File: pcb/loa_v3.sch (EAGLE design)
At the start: 111 parts, among them IC1 STM32F10XVXT6, IC2 M25P80MW, IC3 NAND_FLASH, IC4 MCP1825S-1202E/DB, IC5 NCP3170, IC6 AD7266SU, Q2 50.000, Q3 25.000, U1 6SLX9TQG144, X3 MINI-USB

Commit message: Cleanup
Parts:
- JP8: value (none) -> GND
- SJ2: value (none) -> WP
- SJ3: value (none) -> AGND-GND
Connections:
- net N$37 renamed VDDA
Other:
- moved on the sheet: R12, R13

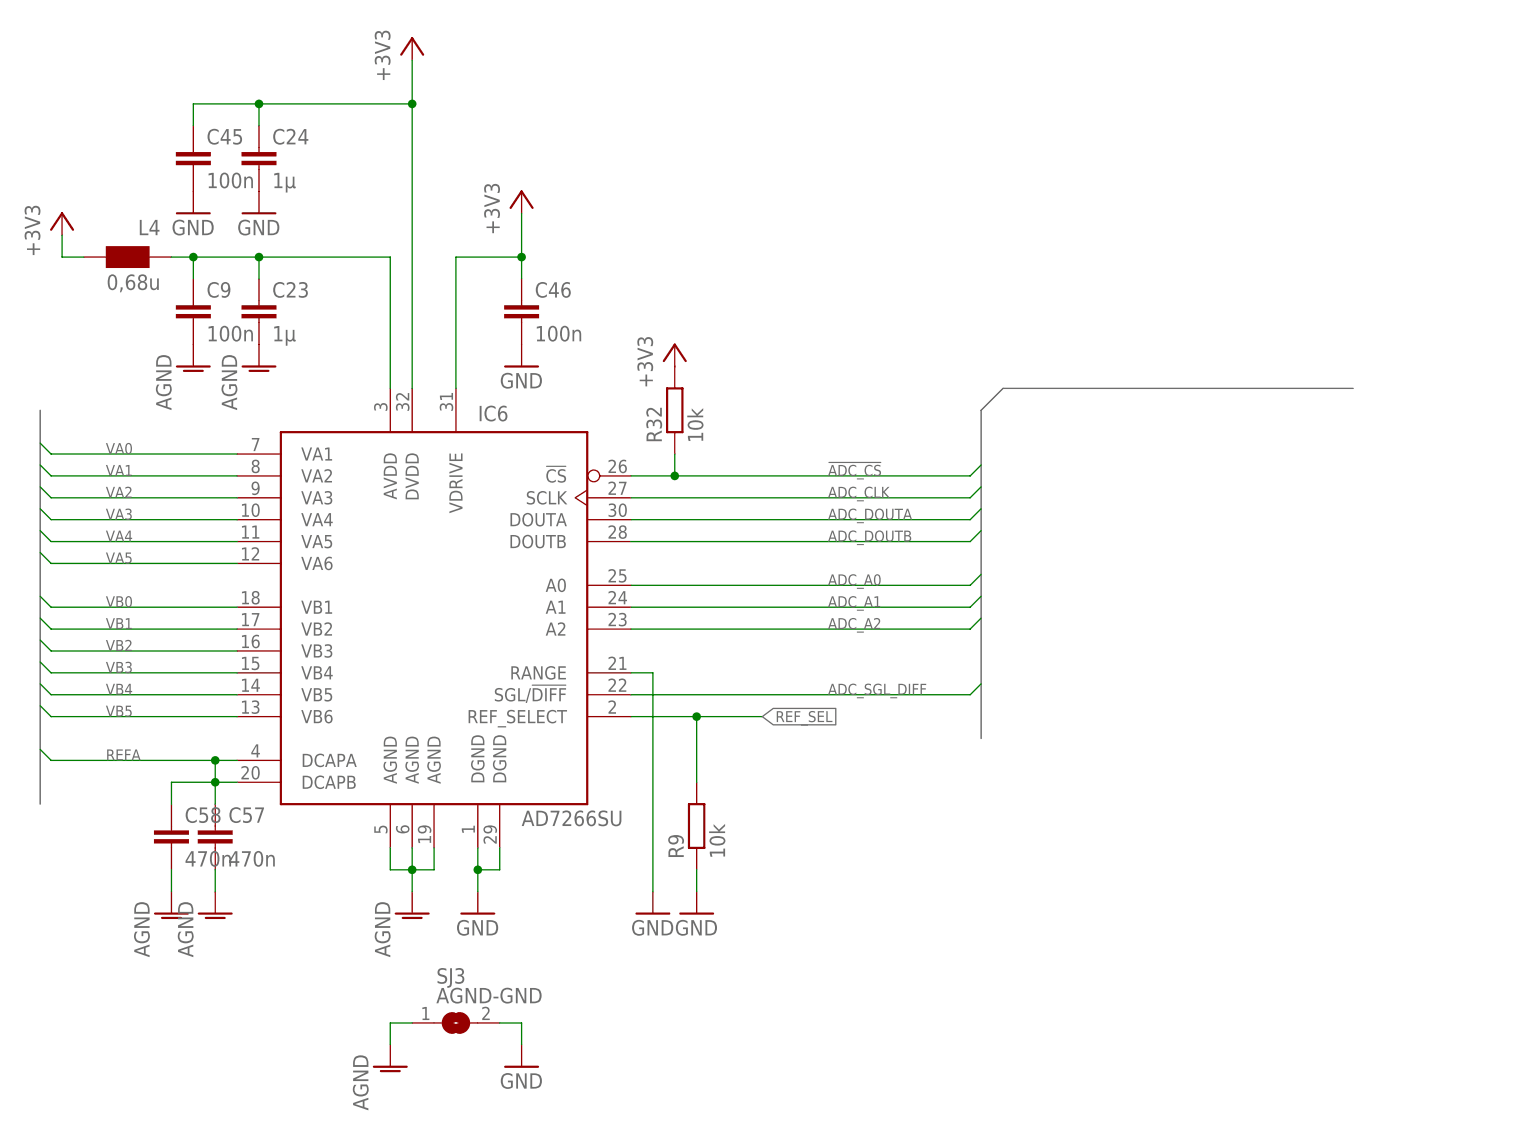
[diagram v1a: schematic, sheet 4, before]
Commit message: Added BOM attributes
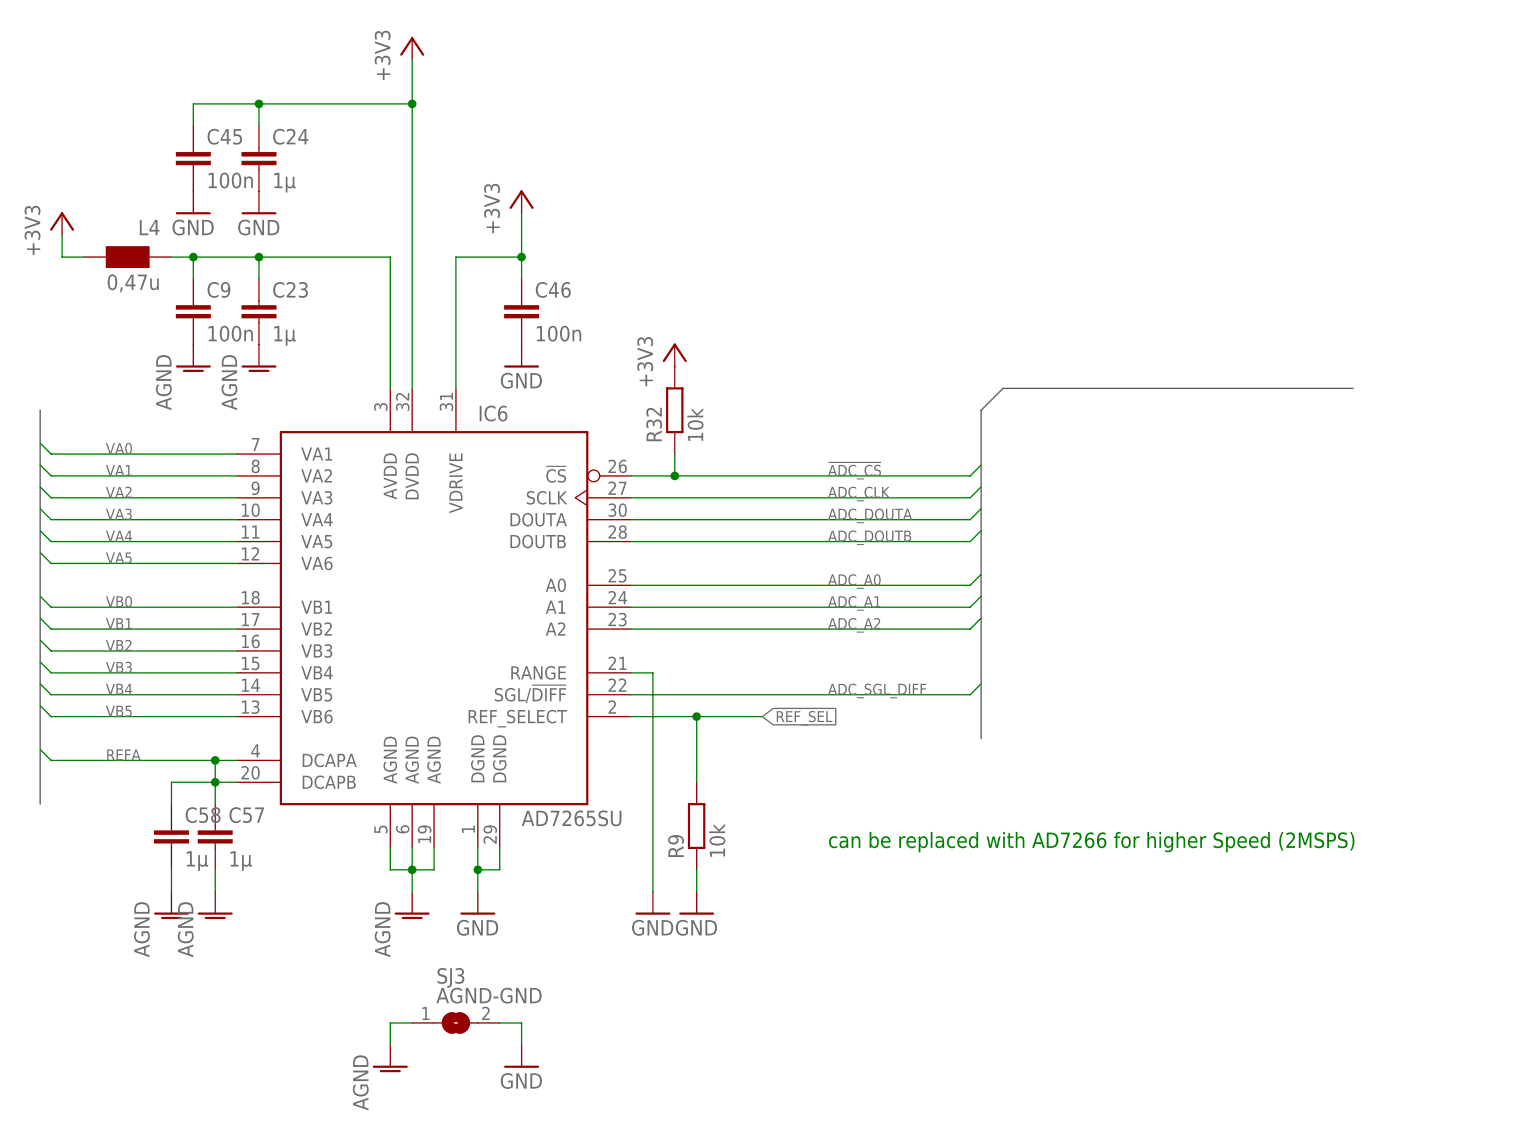
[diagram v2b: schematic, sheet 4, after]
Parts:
- C23, C24, C48, C63, C65: REICHELT# (none) -> X7R-G0805 1,0/25
- C47, C61: REICHELT# (none) -> X5R-G0805 4,7
- C52: REICHELT# (none) -> SMD TAN.22/6,3
- C57, C58: value 470n -> 1µ; REICHELT# (none) -> X7R-G0805 1,0/25
- C6: REICHELT# (none) -> SMD TAN.22/20
- C62, C64: REICHELT# (none) -> X7R-G0603 1,0N
- C66, C67: REICHELT# (none) -> X7R-G0805 2,2/25
- C7, C8: REICHELT# (none) -> SMD TAN.22/6,3; VOLTAGE 20V -> 6,3V
- CC1: REICHELT# (none) -> X7R-G0805 6,8N
- D1: REICHELT# (none) -> MURS 140 SMD
- IC1: DIGIKEY# (none) -> 497-11605-ND
- IC2: DIGIKEY# (none) -> M25P80-VMN6TPCT-ND
- IC3: value NAND_FLASH -> S34ML04G100TFI000; DIGIKEY# (none) -> 1274-1042-ND; MANF (none) -> Spansion
- IC4: DIGIKEY# (none) -> MCP1825S-1202E/DB-ND
- IC5: DIGIKEY# (none) -> NCP3170ADR2GOSCT-ND
- IC6: value AD7266SU -> AD7265SU; DIGIKEY# (none) -> AD7265BSUZ-ND
- JP11, JP2: REICHELT# (none) -> WSL 10G
- JP5: DIGIKEY# (none) -> WM3295CT-ND
- L2, L4: value 0,68u -> 0,47u; REICHELT# (none) -> JCI 2012 0,47µ
- L3: REICHELT# (none) -> L-PISG 4,7µ
- LED1: REICHELT# (none) -> SMD-LED 0805 RT
- LED10: REICHELT# (none) -> SMD-LED 0805 BL
- LED2: value Red -> Yellow; REICHELT# (none) -> SMD-LED 0805 GE
- LED3, LED9: REICHELT# (none) -> SMD-LED 0805 GN
- Q2: REICHELT# (none) -> XO53 50,00000
- Q3: REICHELT# (none) -> XO53 25,00000
- R27: DIGIKEY# (none) -> 311-24.9KCRCT-ND
- R30: DIGIKEY# (none) -> 311-8.06KCRCT-ND
- RC1: DIGIKEY# (none) -> 311-4.99KCRCT-ND
- RN3, RN4, RN6, RN7: REICHELT# (none) -> BCN16 100
- S2: REICHELT# (none) -> TASTER 9315
- U1: DIGIKEY# (none) -> 122-1745-ND
- X3: REICHELT# (none) -> USB BWM SMD
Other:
- note added: "can be replaced with AD7266 for higher Speed (2MSPS)"
